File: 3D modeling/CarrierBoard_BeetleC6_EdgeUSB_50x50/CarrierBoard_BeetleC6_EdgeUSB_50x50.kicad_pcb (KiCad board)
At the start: 2 copper layers, 50 x 50 mm, 12 parts

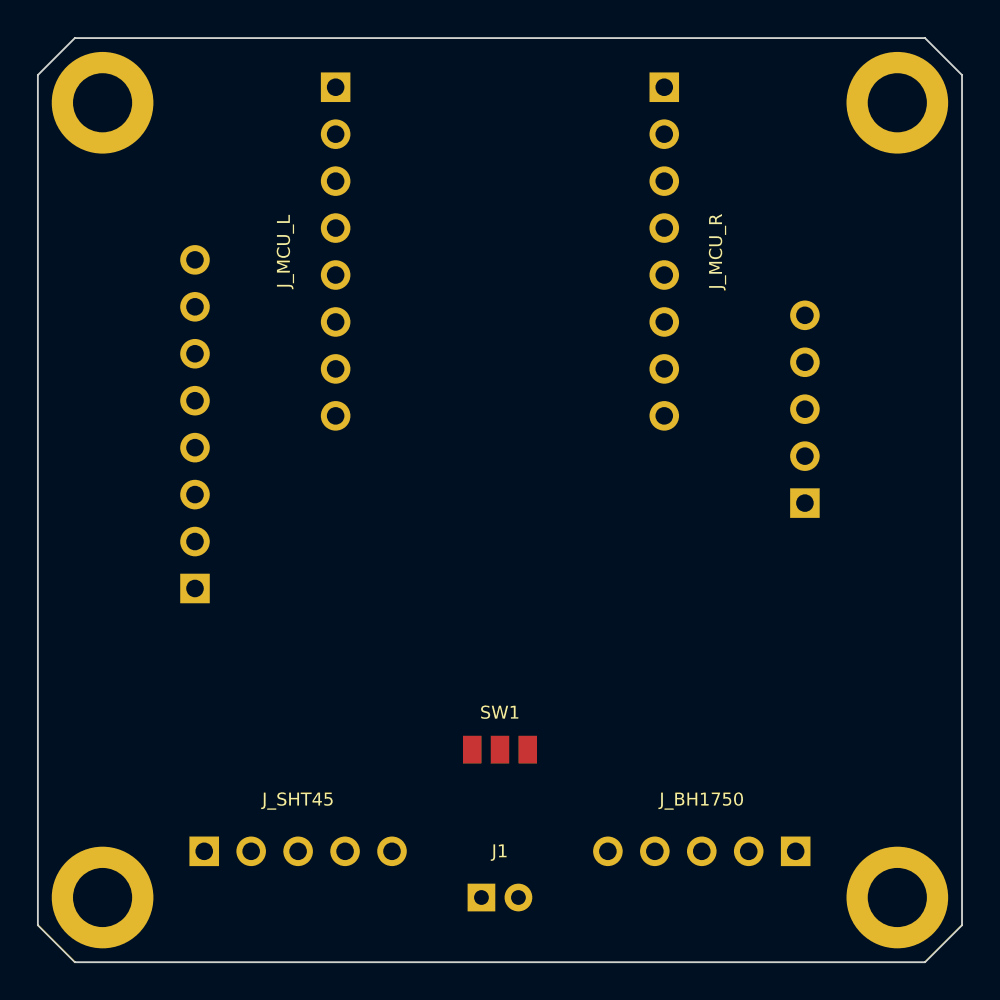
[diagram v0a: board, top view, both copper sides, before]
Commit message: feat(hardware): Refine carrier board with aesthetic orthogonal routing, silkscreen labels, and clean JLCPCB Gerbers
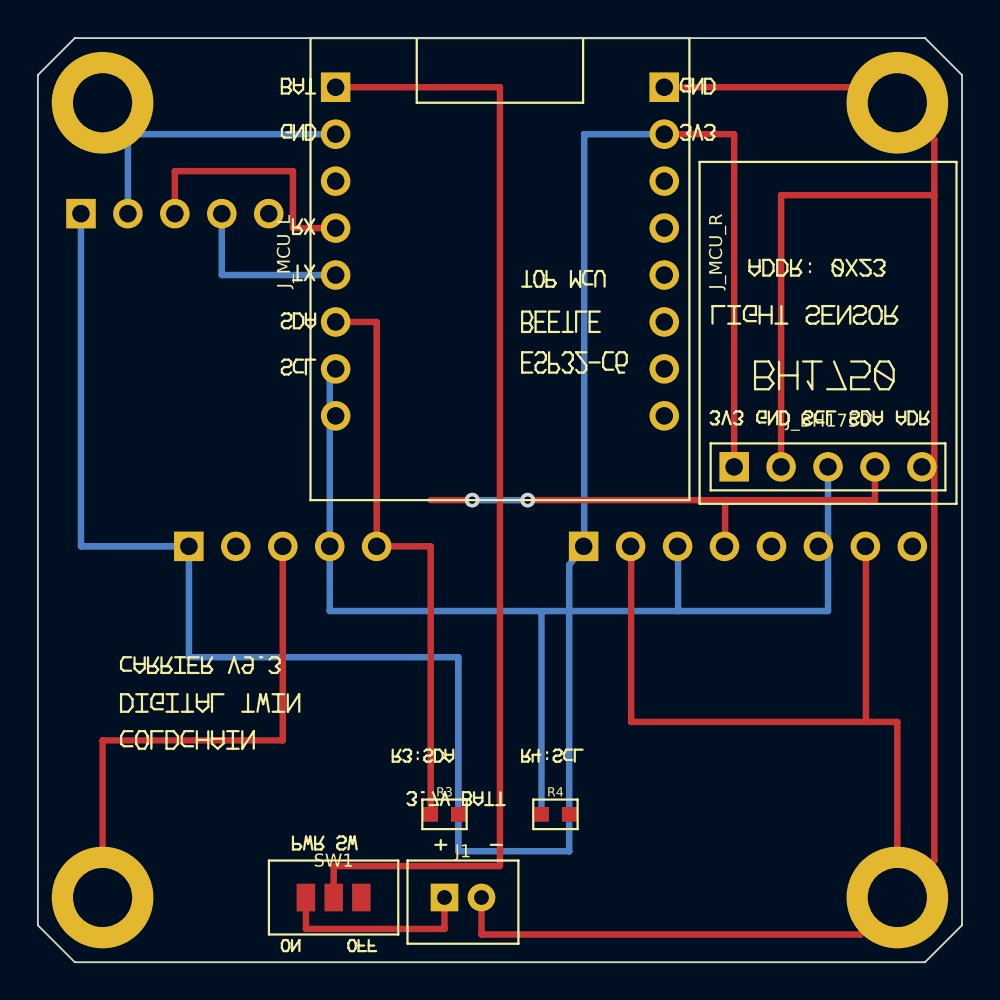
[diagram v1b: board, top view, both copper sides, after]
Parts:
- removed the J_GPS at (141.5, 120.1)
- added J_GPS: , Connector_PinHeader_2.54mm:PinHeader_1x05_P2.54mm_Horizontal, B.Cu at (107.4, 109.5)
- added R3: , Resistor_SMD:R_0603_1608Metric, F.Cu at (122.0, 142.0)
- added R4: , Resistor_SMD:R_0603_1608Metric, F.Cu at (128.0, 142.0)
- J_GY521: footprint Connector_PinHeader_2.54mm:PinHeader_1x08_P2.54mm_Vertical -> Connector_PinHeader_2.54mm:PinHeader_1x08_P2.54mm_Horizontal
- J_SHT45: moved to B.Cu
- moved J_GY521 30.6 mm to (138.4, 127.5)
- moved J_BH1750 21.9 mm to (142.8, 123.2)
- moved J_SHT45 16.5 mm to (113.2, 127.5)
- moved SW1 12.0 mm to (116.0, 146.5)
- moved J1 2.00 mm to (123.0, 146.5)
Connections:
- J_BH1750 pad 1: GND -> 3V3
- J_BH1750 pad 2: I2C_SDA -> GND
- J_BH1750 pad 4: GND -> I2C_SDA
- J_BH1750 pad 5: 3V3 -> GND
- J_GY521 pad 1: (no net) -> 3V3
- J_GY521 pad 3: (no net) -> I2C_SCL
- J_GY521 pad 4: (no net) -> I2C_SDA
- J_GY521 pad 5: I2C_SDA -> (no net)
- J_GY521 pad 6: I2C_SCL -> (no net)
- J_GY521 pad 8: 3V3 -> (no net)
- J_SHT45 pad 2: GND -> (no net)
- J_SHT45 pad 3: I2C_SCL -> GND
- J_SHT45 pad 4: I2C_SDA -> I2C_SCL
- J_SHT45 pad 5: (no net) -> I2C_SDA
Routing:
- net GND: track 0.00 -> 196.6 mm
- net 3V3: track 0.00 -> 126.1 mm
- net I2C_SCL: track 0.00 -> 62.7 mm
- net BAT: track 0.00 -> 61.7 mm
- net I2C_SDA: track 0.00 -> 60.1 mm, vias 0 -> 2
- net GPS_RX: track 0.00 -> 14.1 mm
- net BAT+: track 0.00 -> 10.9 mm
- net GPS_TX: track 0.00 -> 9.48 mm
